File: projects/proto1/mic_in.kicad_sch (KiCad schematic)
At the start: 22 parts, among them J13 MS_SEL, U54 MC33078

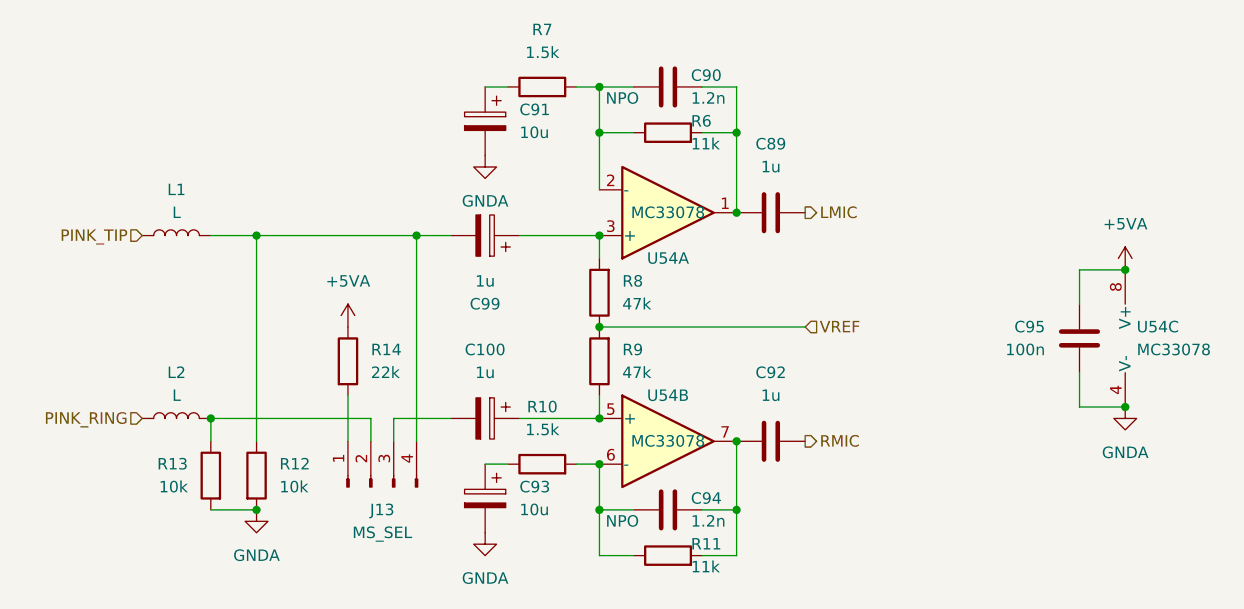
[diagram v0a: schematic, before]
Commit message: Renamed CMC to SCU, changed verification method to cocotb, and modified pcb schematic
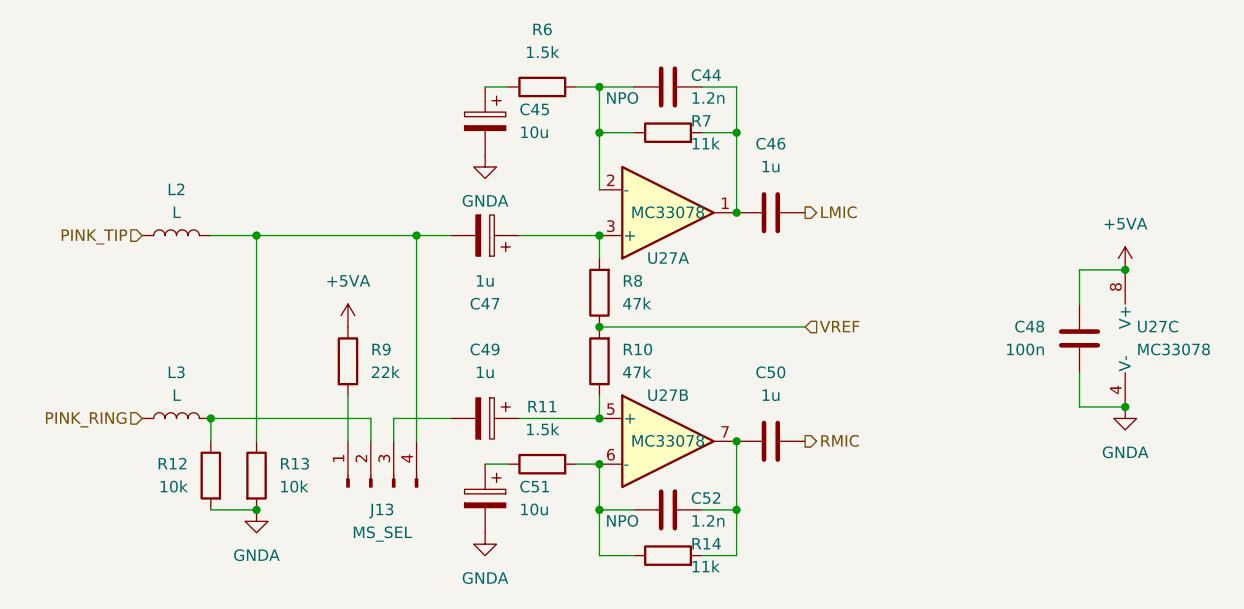
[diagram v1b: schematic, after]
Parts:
- renumbered C90 to C44, C91 to C45, C89 to C46, C99 to C47, C95 to C48, C100 to C49, C92 to C50, C93 to C51, C94 to C52, L1 to L2, L2 to L3, R9 to R10, R10 to R11, R13 to R12, R12 to R13, R11 to R14, R7 to R6, R6 to R7, R14 to R9, U54 to U27
